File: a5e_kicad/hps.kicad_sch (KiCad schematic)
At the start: 18 parts, among them U11 THGAMVG7T13BAIL, U7 A5EB013B-B23B

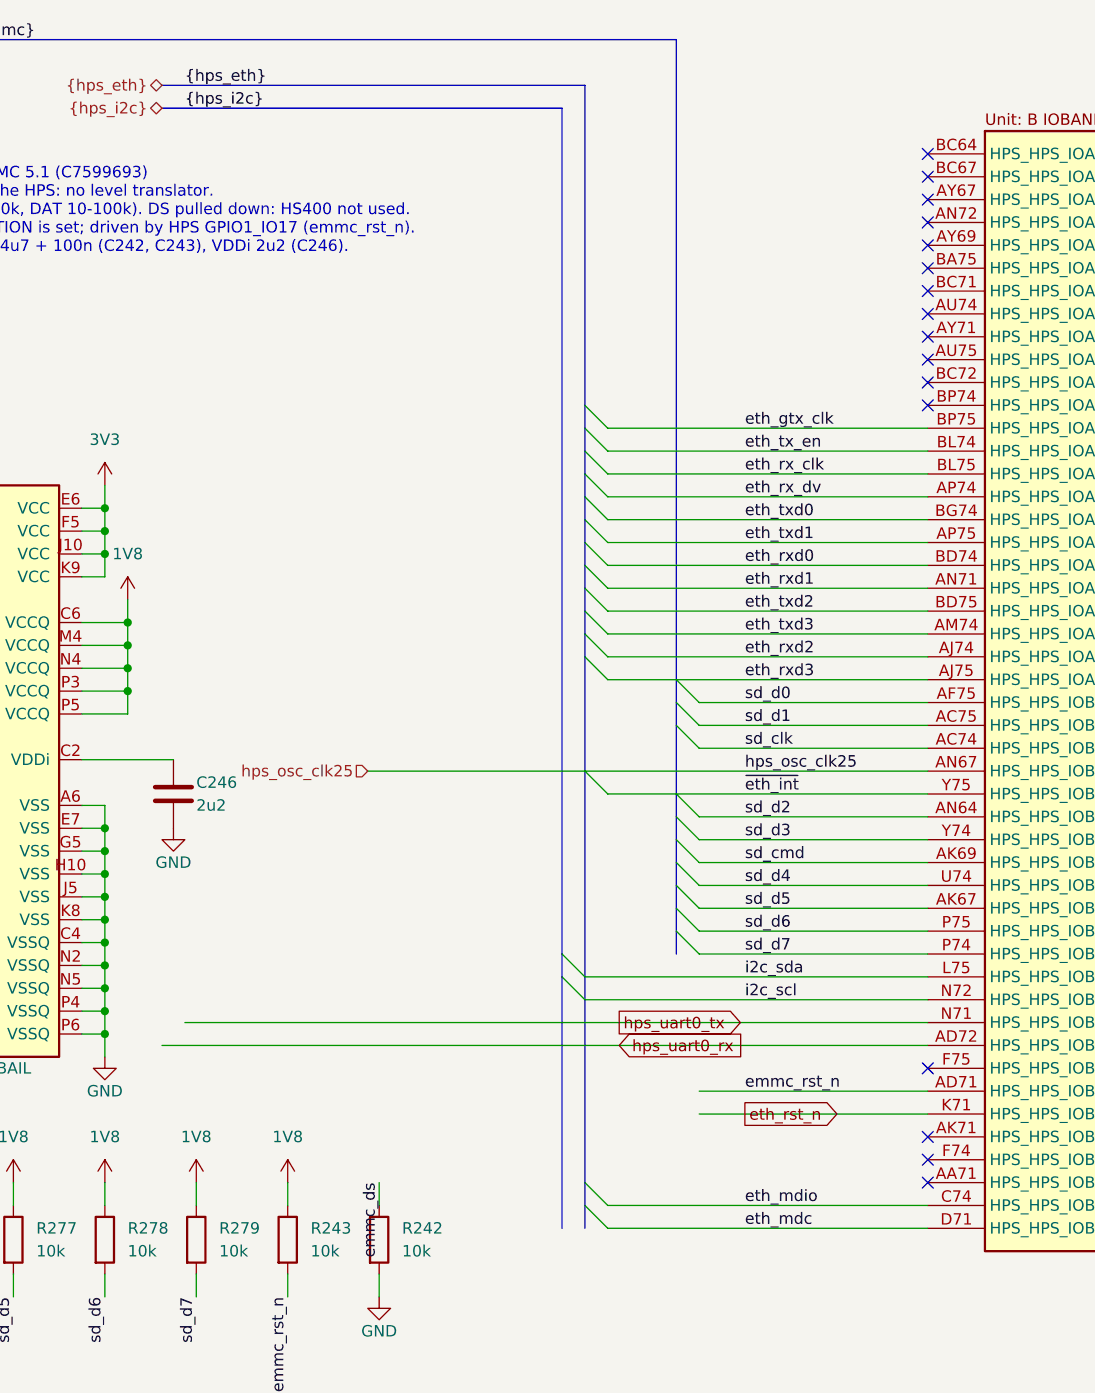
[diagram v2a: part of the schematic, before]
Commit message: HPS pin mux: SD/MMC on IOA_1-12, Ethernet on EMAC2 (IOB_13-24) so they no longer cross
MDIO2 on IOB_9/10, UART0 on IOA_23/24, I2C1 on IOB_7/8, eth_rst_n on IOB_2, emmc_rst_n on IOA_13.
Quartus 26.1.1 fit with the full HPS IO exported: 0 errors, all 32 pins match the netlist (HPS_PINMUX.md).
PCB synced (parity 0); old SD/PHY copper at the U7 HPS balls still needs rerouting.
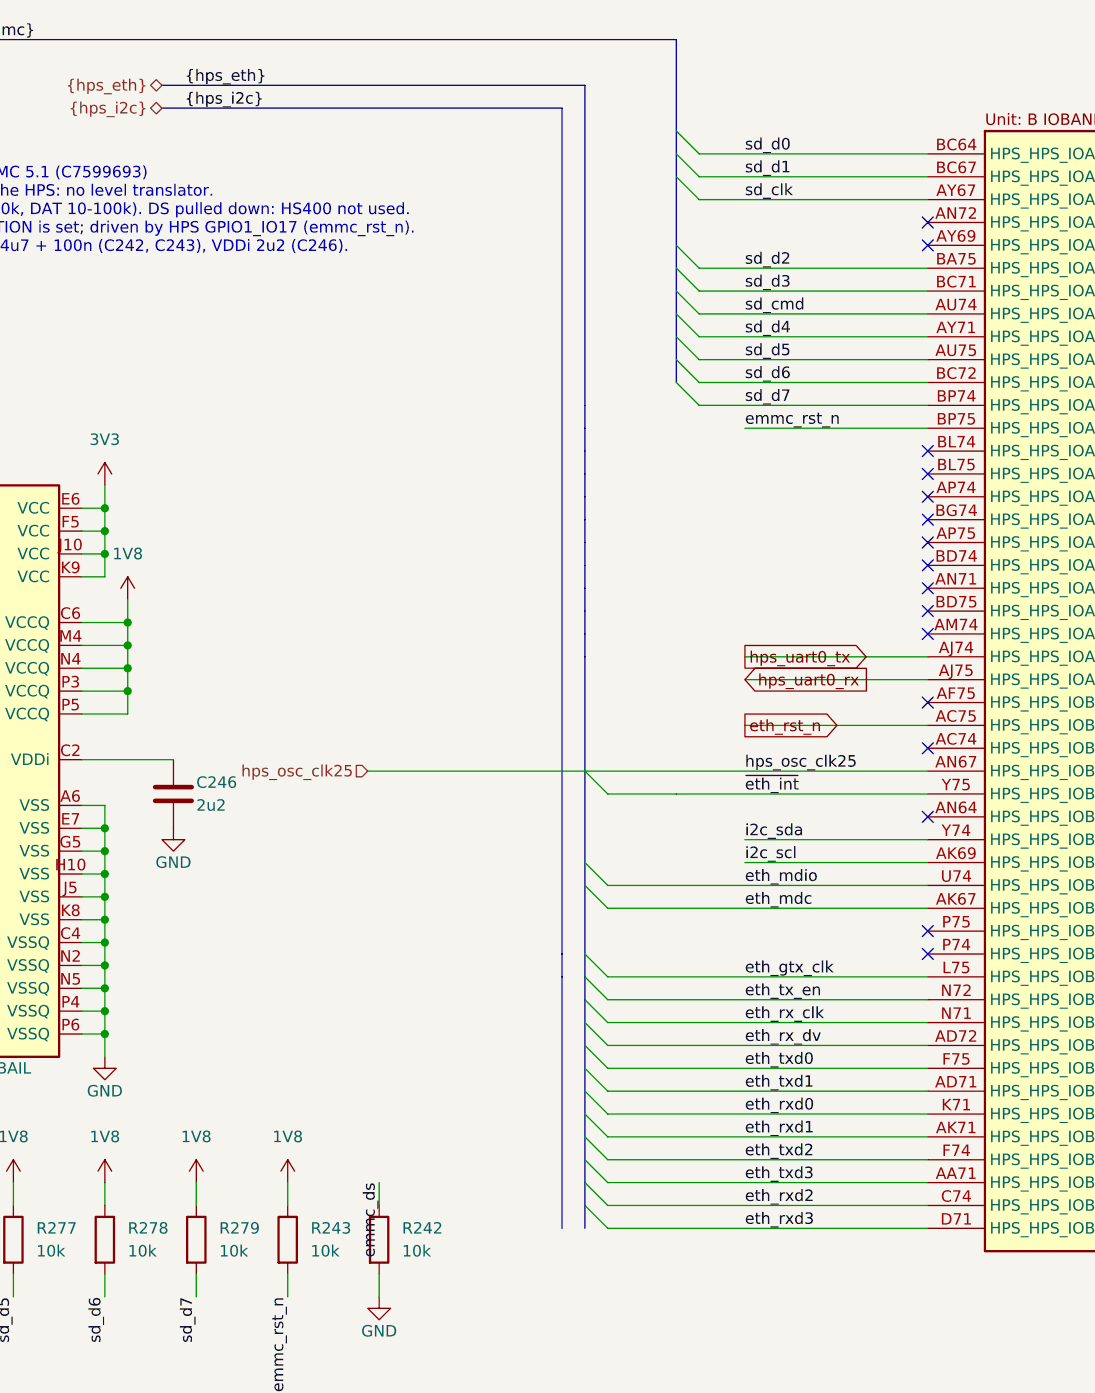
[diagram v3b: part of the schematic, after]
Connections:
- net emmc_rst_n: now also U7.BP75 (HPS_HPS_IOA_13_GPIO0_IO12); no longer U7.AD71 (HPS_HPS_IOB_18_GPIO1_IO17)
- net eth_gtx_clk: now also U7.L75 (HPS_HPS_IOB_13_GPIO1_IO12); no longer U7.BP75 (HPS_HPS_IOA_13_GPIO0_IO12)
- net eth_mdc: now also U7.AK67 (HPS_HPS_IOB_10_GPIO1_IO9); no longer U7.D71 (HPS_HPS_IOB_24_GPIO1_IO23)
- net eth_mdio: now also U7.U74 (HPS_HPS_IOB_9_GPIO1_IO8); no longer U7.C74 (HPS_HPS_IOB_23_GPIO1_IO22)
- net eth_rst_n: now also U7.AC75 (HPS_HPS_IOB_2_GPIO1_IO1); no longer U7.K71 (HPS_HPS_IOB_19_GPIO1_IO18)
- net eth_rx_clk: now also U7.N71 (HPS_HPS_IOB_15_GPIO1_IO14); no longer U7.BL75 (HPS_HPS_IOA_15_GPIO0_IO14_NAND_CE_N_USB1_DIR_EMAC0_RX_CLK_TRACE_D8)
- net eth_rx_dv: now also U7.AD72 (HPS_HPS_IOB_16_GPIO1_IO15); no longer U7.AP74 (HPS_HPS_IOA_16_GPIO0_IO15)
- net eth_rxd0: now also U7.K71 (HPS_HPS_IOB_19_GPIO1_IO18); no longer U7.BD74 (HPS_HPS_IOA_19_GPIO0_IO18)
- net eth_rxd1: now also U7.AK71 (HPS_HPS_IOB_20_GPIO1_IO19); no longer U7.AN71 (HPS_HPS_IOA_20_GPIO0_IO19)
- net eth_rxd2: now also U7.C74 (HPS_HPS_IOB_23_GPIO1_IO22); no longer U7.AJ74 (HPS_HPS_IOA_23_GPIO0_IO22)
- net eth_rxd3: now also U7.D71 (HPS_HPS_IOB_24_GPIO1_IO23); no longer U7.AJ75 (HPS_HPS_IOA_24_GPIO0_IO23)
- net eth_tx_en: now also U7.N72 (HPS_HPS_IOB_14_GPIO1_IO13); no longer U7.BL74 (HPS_HPS_IOA_14_GPIO0_IO13)
- net eth_txd0: now also U7.F75 (HPS_HPS_IOB_17_GPIO1_IO16); no longer U7.BG74 (HPS_HPS_IOA_17_GPIO0_IO16)
- net eth_txd1: now also U7.AD71 (HPS_HPS_IOB_18_GPIO1_IO17); no longer U7.AP75 (HPS_HPS_IOA_18_GPIO0_IO17)
- net eth_txd2: now also U7.F74 (HPS_HPS_IOB_21_GPIO1_IO20); no longer U7.BD75 (HPS_HPS_IOA_21_GPIO0_IO20)
- net eth_txd3: now also U7.AA71 (HPS_HPS_IOB_22_GPIO1_IO21); no longer U7.AM74 (HPS_HPS_IOA_22_GPIO0_IO21)
- net hps_uart0_rx: now also U7.AJ75 (HPS_HPS_IOA_24_GPIO0_IO23); no longer U7.AD72 (HPS_HPS_IOB_16_GPIO1_IO15)
- net hps_uart0_tx: now also U7.AJ74 (HPS_HPS_IOA_23_GPIO0_IO22); no longer U7.N71 (HPS_HPS_IOB_15_GPIO1_IO14)
- net i2c_scl: now also U7.AK69 (HPS_HPS_IOB_8_GPIO1_IO7); no longer U7.N72 (HPS_HPS_IOB_14_GPIO1_IO13)
- net i2c_sda: now also U7.Y74 (HPS_HPS_IOB_7_GPIO1_IO6); no longer U7.L75 (HPS_HPS_IOB_13_GPIO1_IO12)
- net sd_clk: now also U7.AY67 (HPS_HPS_IOA_3_GPIO0_IO2); no longer U7.AC74 (HPS_HPS_IOB_3_GPIO1_IO2)
- net sd_cmd: now also U7.AU74 (HPS_HPS_IOA_8_GPIO0_IO7); no longer U7.AK69 (HPS_HPS_IOB_8_GPIO1_IO7)
- net sd_d0: now also U7.BC64 (HPS_HPS_IOA_1_GPIO0_IO0); no longer U7.AF75 (HPS_HPS_IOB_1_GPIO1_IO0)
- net sd_d1: now also U7.BC67 (HPS_HPS_IOA_2_GPIO0_IO1); no longer U7.AC75 (HPS_HPS_IOB_2_GPIO1_IO1)
- net sd_d2: now also U7.BA75 (HPS_HPS_IOA_6_GPIO0_IO5); no longer U7.AN64 (HPS_HPS_IOB_6_GPIO1_IO5)
- net sd_d3: now also U7.BC71 (HPS_HPS_IOA_7_GPIO0_IO6); no longer U7.Y74 (HPS_HPS_IOB_7_GPIO1_IO6)
- net sd_d4: now also U7.AY71 (HPS_HPS_IOA_9_GPIO0_IO8); no longer U7.U74 (HPS_HPS_IOB_9_GPIO1_IO8)
- net sd_d5: now also U7.AU75 (HPS_HPS_IOA_10_GPIO0_IO9); no longer U7.AK67 (HPS_HPS_IOB_10_GPIO1_IO9)
- net sd_d6: now also U7.BC72 (HPS_HPS_IOA_11_GPIO0_IO10); no longer U7.P75 (HPS_HPS_IOB_11_GPIO1_IO10)
- net sd_d7: now also U7.BP74 (HPS_HPS_IOA_12_GPIO0_IO11); no longer U7.P74 (HPS_HPS_IOB_12_GPIO1_IO11)

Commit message: eMMC DS to HPS_IOA_16 (SDMMC_DATA_STROBE, HS400); delete stale SD/Ethernet copper at U7 HPS
- Schematic: emmc_ds now also goes to U7 AP74 (HPS_IOA_16); R242 stays as the pull-down.
  Quartus fit with SDMMC:DATA_STROBE on IOA_16: 0 errors, strobe on AP74.
- PCB: AP74 pad net set to /HPS/emmc_ds. Deleted 222 segments and 33 vias left over from the
  pin-mux swap: all RGMII/MDIO, eth_rst_n and hps_uart0_tx/rx (1V8 side) routing, plus the old
  SD routing that had become no-net or unused-ball copper.
- DRC: 261 violations (was 331), 312 unconnected (was 304), schematic parity 0. ERC 315 unchanged.
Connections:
- net emmc_ds: now also U7.AP74 (HPS_HPS_IOA_16_GPIO0_IO15)
- no-connect marks 16 -> 15
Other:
- note added: "eMMC: U11 KIOXIA THGAMVG7T13BAIL, 16 GB eMMC 5.1 (C7599693) VCCQ is 1.8 V only and must be the same 1V8 as the HPS: no level translator. CMD/DAT pull-ups 10k to 1V8 (KIOXIA: CMD 4.7-100k, DAT 10-100k). DS to HPS_IOA_16 (SDMMC_DATA_STROBE) for HS400, 10k pull-down R242. RST_n is ignored until EXT_CSD[162] RST_n_FUNCTION is set; driven by HPS GPIO0_IO12 (emmc_rst_n). Decoupling: VCC 4u7 + 220n (C24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"
- note removed: "eMMC: U11 KIOXIA THGAMVG7T13BAIL, 16 GB eMMC 5.1 (C7599693) VCCQ is 1.8 V only and must be the same 1V8 as the HPS: no level translator. CMD/DAT pull-ups 10k to 1V8 (KIOXIA: CMD 4.7-100k, DAT 10-100k). DS pulled down: HS400 not used. RST_n is ignored until EXT_CSD[162] RST_n_FUNCTION is set; driven by HPS GPIO1_IO17 (emmc_rst_n). Decoupling: VCC 4u7 + 220n (C244, C245), VCCQ 4u7 + 100n (C242, C24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"
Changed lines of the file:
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@@
 		)
 	)
-	(text "eMMC: U11 KIOXIA THGAMVG7T13BAIL, 16 GB eMMC 5.1 (C7599693)\nVCCQ is 1.8 V only and must be the same 1V8 as the HPS: no level translator.\nCMD/DAT pull-ups 10k to 1V8 (KIOXIA: CMD 4.7-100k, DAT 10-100k). DS pulled down: HS400 not used.\nRST_n is ignored until EXT_CSD[162] RST_n_FUNCTION is set; driven by HPS GPIO1_IO17 (emmc_rst_n).\nDecoupling: VCC 4u7 + 220n (C244, C245), VCCQ 4u7 + 100n (C242, C243), VDDi 2u2 (C246)."
+	(text "eMMC: U11 KIOXIA THGAMVG7T13BAIL, 16 GB eMMC 5.1 (C7599693)\nVCCQ is 1.8 V only and must be the same 1V8 as the HPS: no level translator.\nCMD/DAT pull-ups 10k to 1V8 (KIOXIA: CMD 4.7-100k, DAT 10-100k). DS to HPS_IOA_16 (SDMMC_DATA_STROBE) for HS400, 10k pull-down R242.\nRST_n is ignored until EXT_CSD[162] RST_n_FUNCTION is set; driven by HPS GPIO0_IO12 (emmc_rst_n).\nDecoupling: VCC 4u7 + 220n (C244, C245), VCCQ 4u7 + 100n (C242, C243), VDDi 2u2 (C246)."
 		(exclude_from_sim no)
 		(at 35.56 38.1 0)
@@
 	(no_connect
 		(at 182.88 67.31)
-	)
-	(no_connect
-		(at 182.88 69.85)
 	)
 	(no_connect
@@
 		(effects
 			(font
+				(size 1.27 1.27)
+			)
+			(justify left bottom)
+		)
+	)
+	(wire
+		(pts
+			(xy 162.56 69.85) (xy 182.88 69.85)
+		)
+		(stroke
+			(width 0)
+			(type default)
+		)
+	)
+	(label "emmc_ds"
+		(at 162.56 69.85 0)
+		(effects
+			(font

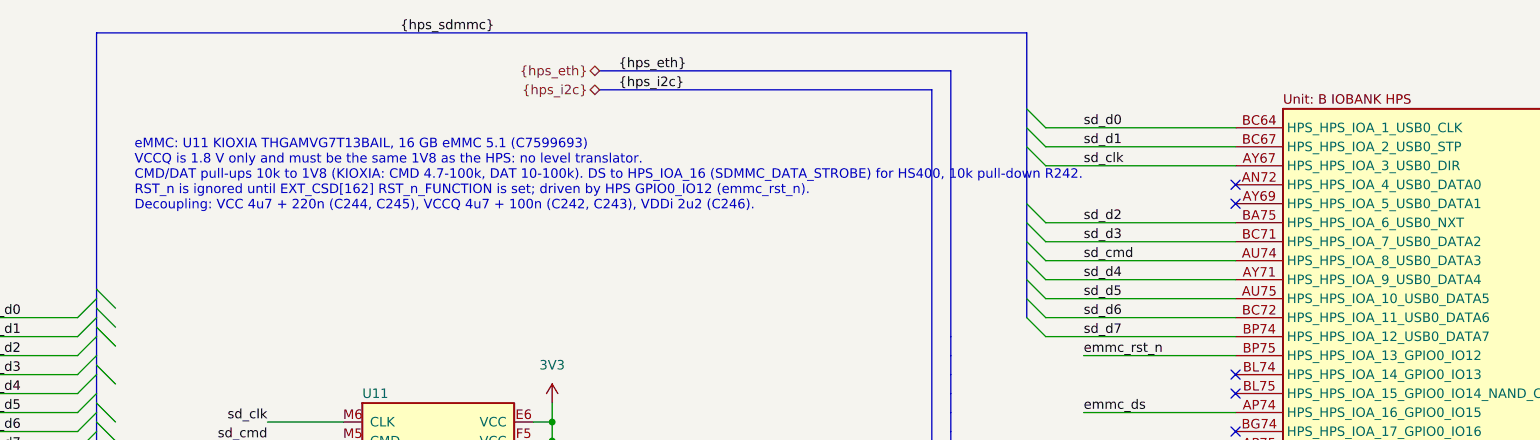
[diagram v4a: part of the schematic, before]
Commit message: eMMC decoupling: 0201 caps on the U11 via-in-pad, 0402 bulk; silkscreen DRC ignored
- C243 100n, C245 220n, C246 2u2 now 0201 (C190183, C76932, C77762); C242/C244 4u7 now
  0402 (C23733, 10 V: a 0201 4u7 loses most of its value at 3.3 V).
- Placed on B.Cu under U11: 0201s directly on the supply/GND ball vias (N4/N5, K9/K8,
  new VDDi via at C2 + C4), 4u7s just outside the ball array with short traces.
- Includes the user's U11 fan-out vias.
- Board ordered without silkscreen: silk_edge_clearance set to ignore (overlap and
  over-copper already were).
- DRC 288 violations, 260 unconnected, schematic parity 0; ERC unchanged at 315.
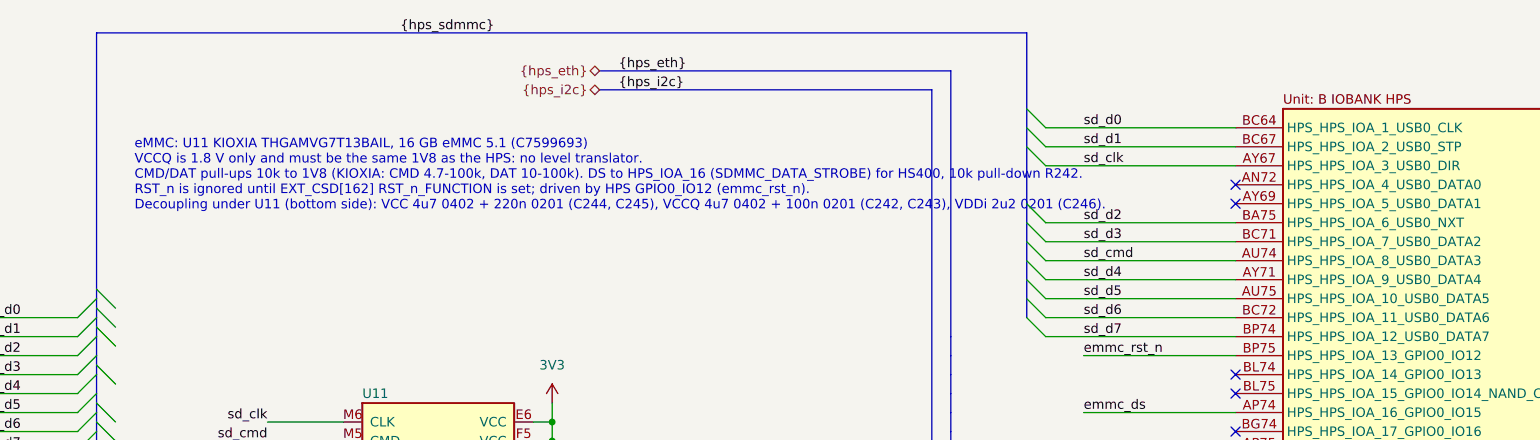
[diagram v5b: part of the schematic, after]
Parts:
- C242, C244: footprint Capacitor_SMD:C_0603_1608Metric -> Capacitor_SMD:C_0402_1005Metric; LCSC C19666 -> C23733
- C243: footprint Capacitor_SMD:C_0402_1005Metric -> Capacitor_SMD:C_0201_0603Metric; LCSC C1525 -> C190183
- C245: footprint Capacitor_SMD:C_0402_1005Metric -> Capacitor_SMD:C_0201_0603Metric; LCSC C16772 -> C76932
- C246: footprint Capacitor_SMD:C_0402_1005Metric -> Capacitor_SMD:C_0201_0603Metric; LCSC C12530 -> C77762
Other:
- note added: "eMMC: U11 KIOXIA THGAMVG7T13BAIL, 16 GB eMMC 5.1 (C7599693) VCCQ is 1.8 V only and must be the same 1V8 as the HPS: no level translator. CMD/DAT pull-ups 10k to 1V8 (KIOXIA: CMD 4.7-100k, DAT 10-100k). DS to HPS_IOA_16 (SDMMC_DATA_STROBE) for HS400, 10k pull-down R242. RST_n is ignored until EXT_CSD[162] RST_n_FUNCTION is set; driven by HPS GPIO0_IO12 (emmc_rst_n). Decoupling under U11 (bottom si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"
- note removed: "eMMC: U11 KIOXIA THGAMVG7T13BAIL, 16 GB eMMC 5.1 (C7599693) VCCQ is 1.8 V only and must be the same 1V8 as the HPS: no level translator. CMD/DAT pull-ups 10k to 1V8 (KIOXIA: CMD 4.7-100k, DAT 10-100k). DS to HPS_IOA_16 (SDMMC_DATA_STROBE) for HS400, 10k pull-down R242. RST_n is ignored until EXT_CSD[162] RST_n_FUNCTION is set; driven by HPS GPIO0_IO12 (emmc_rst_n). Decoupling: VCC 4u7 + 220n (C24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"
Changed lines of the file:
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@@
 			)
 		)
-		(property "Footprint" "Capacitor_SMD:C_0402_1005Metric"
+		(property "Footprint" "Capacitor_SMD:C_0201_0603Metric"
 			(at 99.06 102.87 0)
 			(hide yes)
@@
 			)
 		)
-		(property "LCSC" "C12530"
+		(property "LCSC" "C77762"
 			(at 99.06 102.87 0)
 			(hide yes)
@@
 			)
 		)
-		(property "Footprint" "Capacitor_SMD:C_0603_1608Metric"
+		(property "Footprint" "Capacitor_SMD:C_0402_1005Metric"
 			(at 40.64 185.42 0)
 			(hide yes)
@@
 			)
 		)
-		(property "LCSC" "C19666"
+		(property "LCSC" "C23733"
 			(at 40.64 185.42 0)
 			(hide yes)
@@
 			)
 		)
-		(property "Footprint" "Capacitor_SMD:C_0402_1005Metric"
+		(property "Footprint" "Capacitor_SMD:C_0201_0603Metric"
 			(at 48.26 185.42 0)
 			(hide yes)
@@
 			)
 		)
-		(property "LCSC" "C1525"
+		(property "LCSC" "C190183"
 			(at 48.26 185.42 0)
 			(hide yes)
@@
 			)
 		)
-		(property "Footprint" "Capacitor_SMD:C_0603_1608Metric"
+		(property "Footprint" "Capacitor_SMD:C_0402_1005Metric"
 			(at 66.04 185.42 0)
 			(hide yes)
@@
 			)
 		)
-		(property "LCSC" "C19666"
+		(property "LCSC" "C23733"
 			(at 66.04 185.42 0)
 			(hide yes)
@@
 			)
 		)
-		(property "Footprint" "Capacitor_SMD:C_0402_1005Metric"
+		(property "Footprint" "Capacitor_SMD:C_0201_0603Metric"
 			(at 73.66 185.42 0)
 			(hide yes)
@@
 			)
 		)
-		(property "LCSC" "C16772"
+		(property "LCSC" "C76932"
 			(at 73.66 185.42 0)
 			(hide yes)
@@
 		)
 	)
-	(text "eMMC: U11 KIOXIA THGAMVG7T13BAIL, 16 GB eMMC 5.1 (C7599693)\nVCCQ is 1.8 V only and must be the same 1V8 as the HPS: no level translator.\nCMD/DAT pull-ups 10k to 1V8 (KIOXIA: CMD 4.7-100k, DAT 10-100k). DS to HPS_IOA_16 (SDMMC_DATA_STROBE) for HS400, 10k pull-down R242.\nRST_n is ignored until EXT_CSD[162] RST_n_FUNCTION is set; driven by HPS GPIO0_IO12 (emmc_rst_n).\nDecoupling: VCC 4u7 + 220n (C244, C245), VCCQ 4u7 + 100n (C242, C243), VDDi 2u2 (C246)."
+	(text "eMMC: U11 KIOXIA THGAMVG7T13BAIL, 16 GB eMMC 5.1 (C7599693)\nVCCQ is 1.8 V only and must be the same 1V8 as the HPS: no level translator.\nCMD/DAT pull-ups 10k to 1V8 (KIOXIA: CMD 4.7-100k, DAT 10-100k). DS to HPS_IOA_16 (SDMMC_DATA_STROBE) for HS400, 10k pull-down R242.\nRST_n is ignored until EXT_CSD[162] RST_n_FUNCTION is set; driven by HPS GPIO0_IO12 (emmc_rst_n).\nDecoupling under U11 (bottom side): VCC 4u7 0402 + 220n 0201 (C244, C245), VCCQ 4u7 0402 + 100n 0201 (C242, C243), VDDi 2u2 0201 (C246)."
 		(exclude_from_sim no)
 		(at 35.56 38.1 0)
